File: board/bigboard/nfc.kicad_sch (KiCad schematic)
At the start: 3 parts

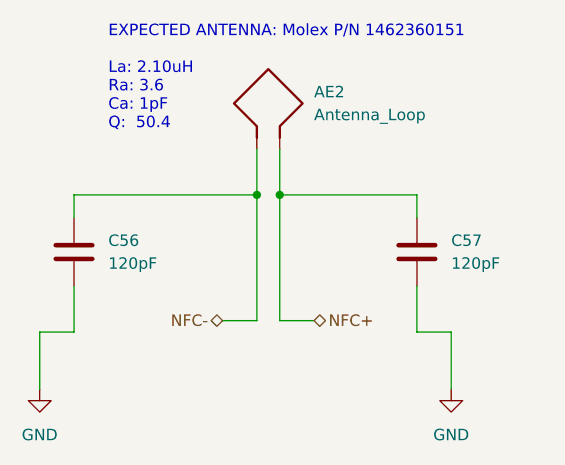
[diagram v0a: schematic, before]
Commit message: Manufactured version of bigboard
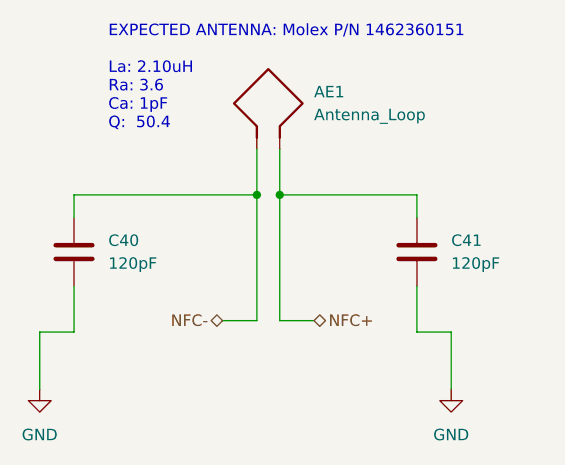
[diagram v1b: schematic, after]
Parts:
- C40: renamed from C56; MPN (none) -> GRM0335C1H121JA01J
- C41: renamed from C57; MPN (none) -> GRM0335C1H121JA01J
- renumbered AE2 to AE1
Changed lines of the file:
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@@
   (symbol (lib_id "power:GND") (at 165.1 120.65 0) (unit 1)
     (in_bom yes) (on_board yes) (fields_autoplaced)
-    (property "Reference" "#PWR052" (id 0) (at 165.1 127 0)
+    (property "Reference" "#PWR048" (id 0) (at 165.1 127 0)
       (effects (font (size 1.27 1.27)) hide)
     )
@@
   (symbol (lib_id "Device:C") (at 161.29 105.41 0) (unit 1)
     (in_bom yes) (on_board yes) (fields_autoplaced)
-    (property "Reference" "C57" (id 0) (at 165.1 104.1399 0)
+    (property "Reference" "C41" (id 0) (at 165.1 104.1399 0)
       (effects (font (size 1.27 1.27)) (justify left))
     )
@@
       (effects (font (size 1.27 1.27)) hide)
     )
+    (property "MPN" "GRM0335C1H121JA01J" (id 5) (at 161.29 105.41 0)
+      (effects (font (size 1.27 1.27)) hide)
+    )
     (pin "1")
     (pin "2")
@@
   (symbol (lib_id "power:GND") (at 119.38 120.65 0) (unit 1)
     (in_bom yes) (on_board yes) (fields_autoplaced)
-    (property "Reference" "#PWR051" (id 0) (at 119.38 127 0)
+    (property "Reference" "#PWR047" (id 0) (at 119.38 127 0)
       (effects (font (size 1.27 1.27)) hide)
     )
@@
   (symbol (lib_id "Device:C") (at 123.19 105.41 0) (unit 1)
     (in_bom yes) (on_board yes) (fields_autoplaced)
-    (property "Reference" "C56" (id 0) (at 127 104.1399 0)
+    (property "Reference" "C40" (id 0) (at 127 104.1399 0)
       (effects (font (size 1.27 1.27)) (justify left))
     )
@@
       (effects (font (size 1.27 1.27)) hide)
     )
+    (property "MPN" "GRM0335C1H121JA01J" (id 5) (at 123.19 105.41 0)
+      (effects (font (size 1.27 1.27)) hide)
+    )
     (pin "1")
     (pin "2")
@@
   (symbol (lib_id "Device:Antenna_Loop") (at 143.51 88.9 0) (unit 1)
     (in_bom yes) (on_board yes) (fields_autoplaced)
-    (property "Reference" "AE2" (id 0) (at 149.86 87.6299 0)
+    (property "Reference" "AE1" (id 0) (at 149.86 87.6299 0)
       (effects (font (size 1.27 1.27)) (justify left))
     )
